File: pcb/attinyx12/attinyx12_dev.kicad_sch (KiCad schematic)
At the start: 28 parts, among them J1 USB_C_Receptacle_USB2.0_16P, J2 Conn_01x06, J3 Conn_01x06, U1 LM321, U2 ATtiny212-SS, U3 CH342K

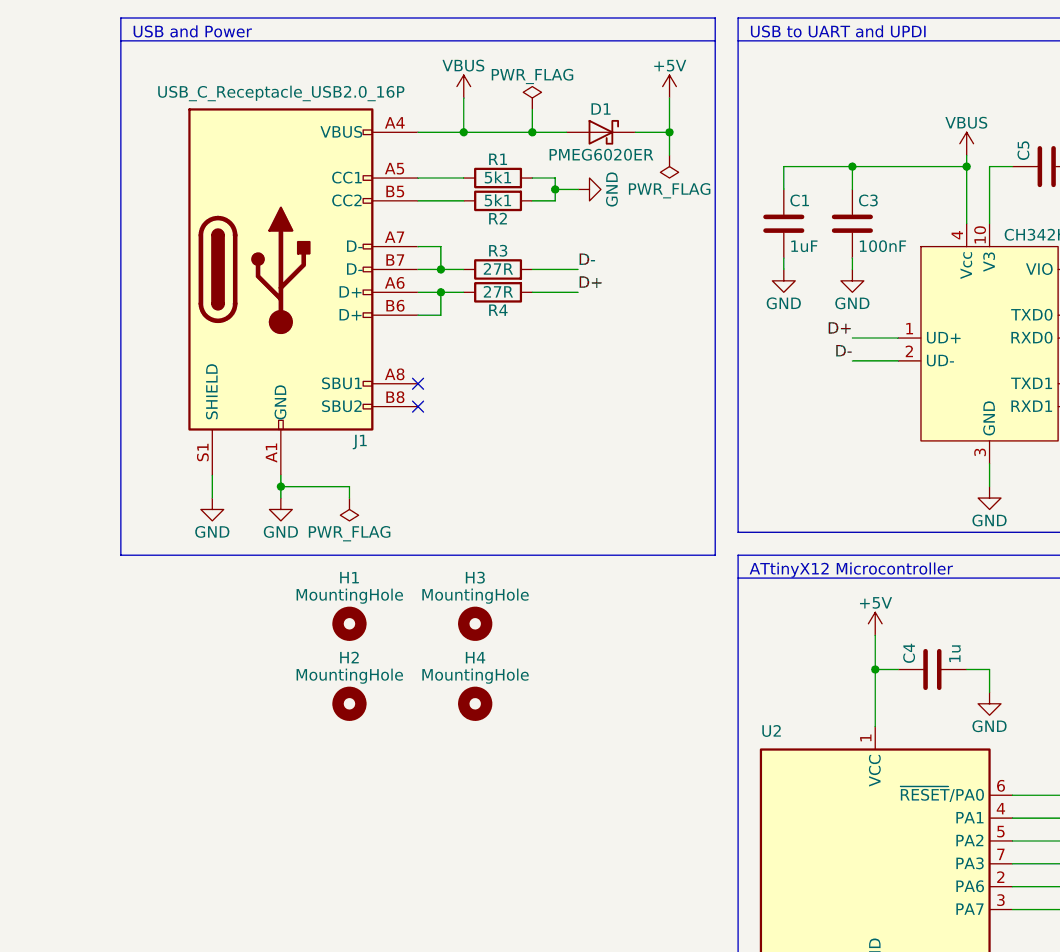
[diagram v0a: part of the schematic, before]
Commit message: polyfuse and TVS+ESD for USB
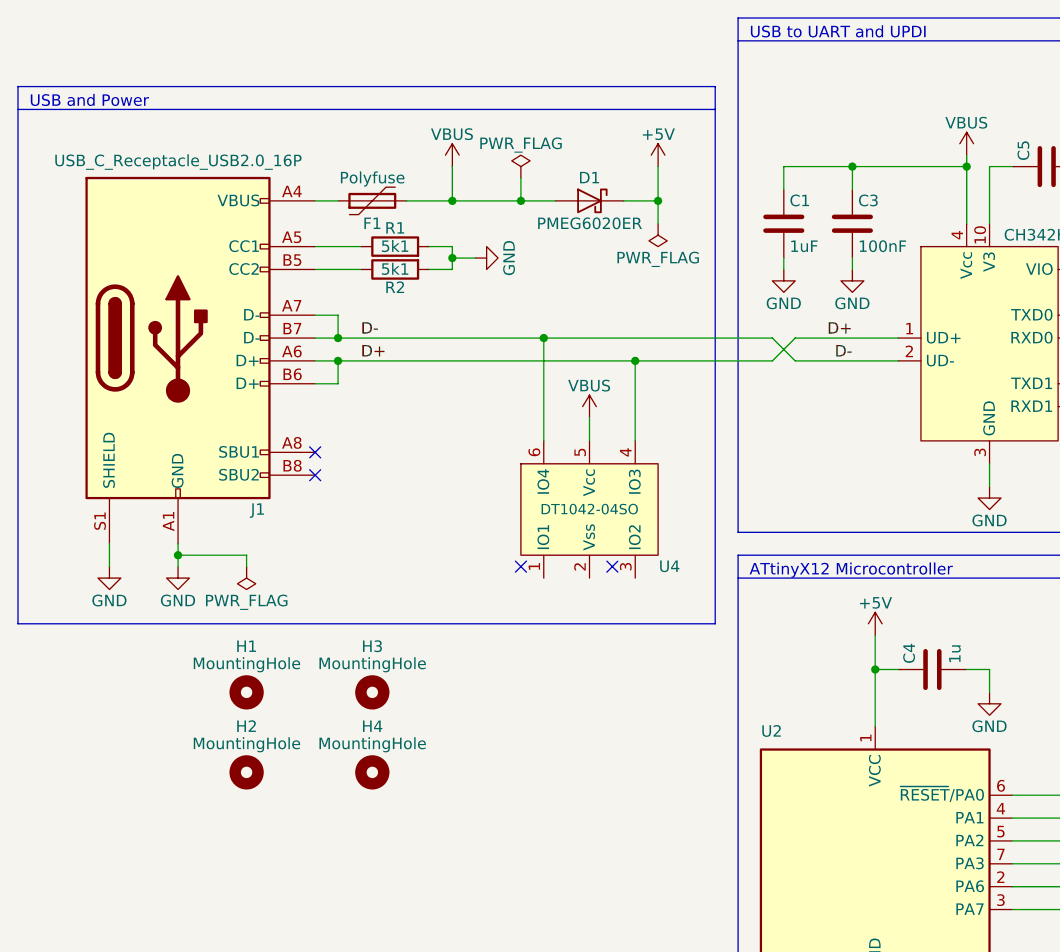
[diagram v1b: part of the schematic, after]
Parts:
- removed R3, R4: 27R, Resistor_SMD:R_0603_1608Metric, symbol Device:R
- added F1: Polyfuse, Fuse:Fuse_0805_2012Metric, symbol Device:Polyfuse
- added U4: DT1042-04SO, Package_TO_SOT_SMD:SOT-23-6, symbol pl_TVS:DT1042-04SO
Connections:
- net D+: now also J1.A6 (D+), J1.B6 (D+), U4.4 (IO3)
- net D-: now also J1.A7 (D-), J1.B7 (D-), U4.6 (IO4)
- net VBUS: now also F1.2, U4.5 (Vcc); no longer J1.A4 (VBUS), J1.A9 (VBUS), J1.B4 (VBUS), J1.B9 (VBUS)
- new net: F1.1, J1.A4 (VBUS), J1.A9 (VBUS), J1.B4 (VBUS), J1.B9 (VBUS)
- no-connect marks 2 -> 4
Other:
- moved on the sheet: D1, H1, H2, H3, H4, J1, R1, R2

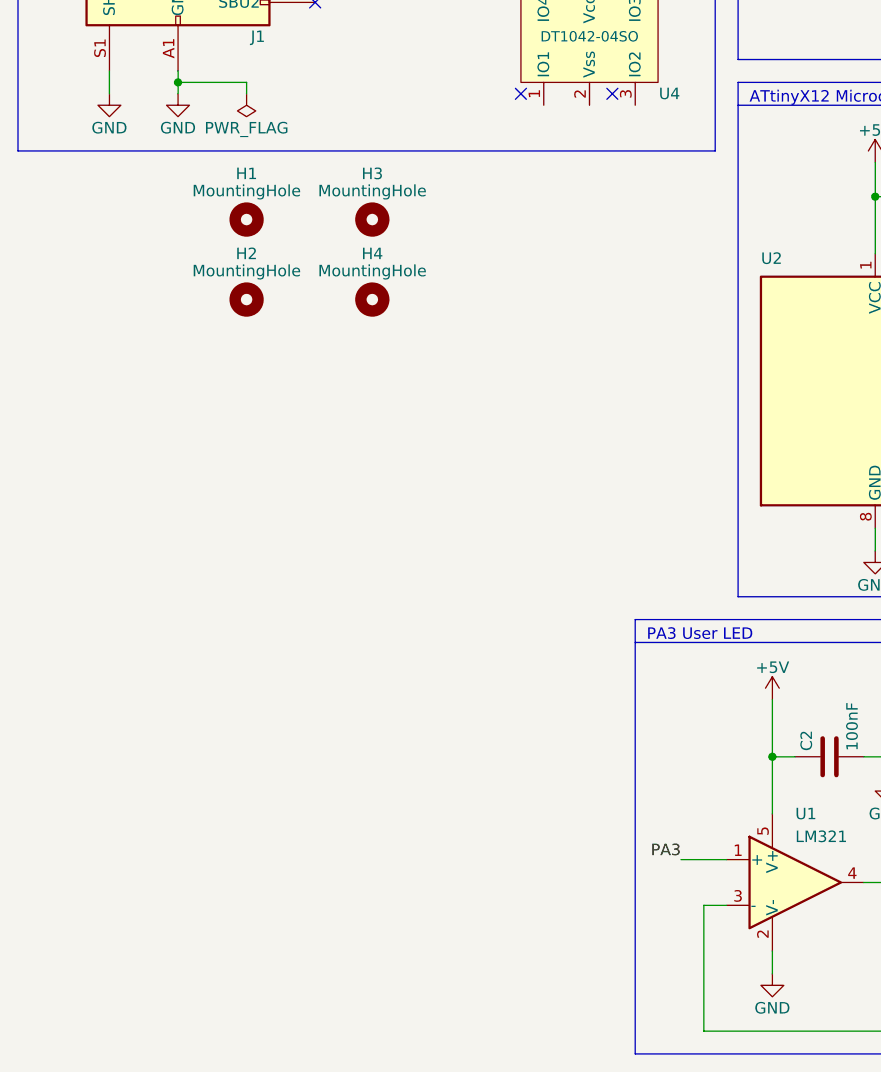
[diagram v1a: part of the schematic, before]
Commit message: add power indicator LED
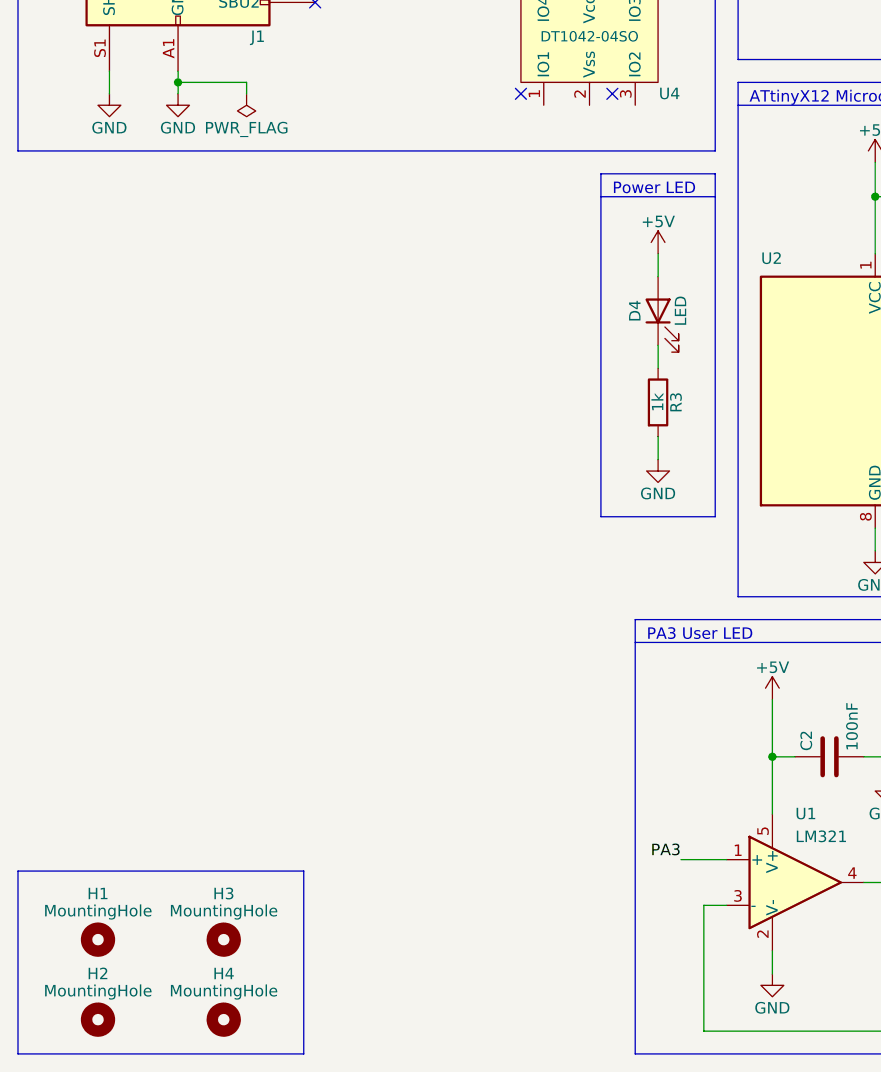
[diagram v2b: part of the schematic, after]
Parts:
- added D4: LED, LED_SMD:LED_0603_1608Metric, symbol Device:LED
- added R3: 1k, Resistor_SMD:R_0603_1608Metric, symbol Device:R
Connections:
- net +5V: now also D4.2 (A)
- net GND: now also R3.2
- new net: D4.1 (K), R3.1
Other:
- note added: "Power LED"
- moved on the sheet: H1, H2, H3, H4

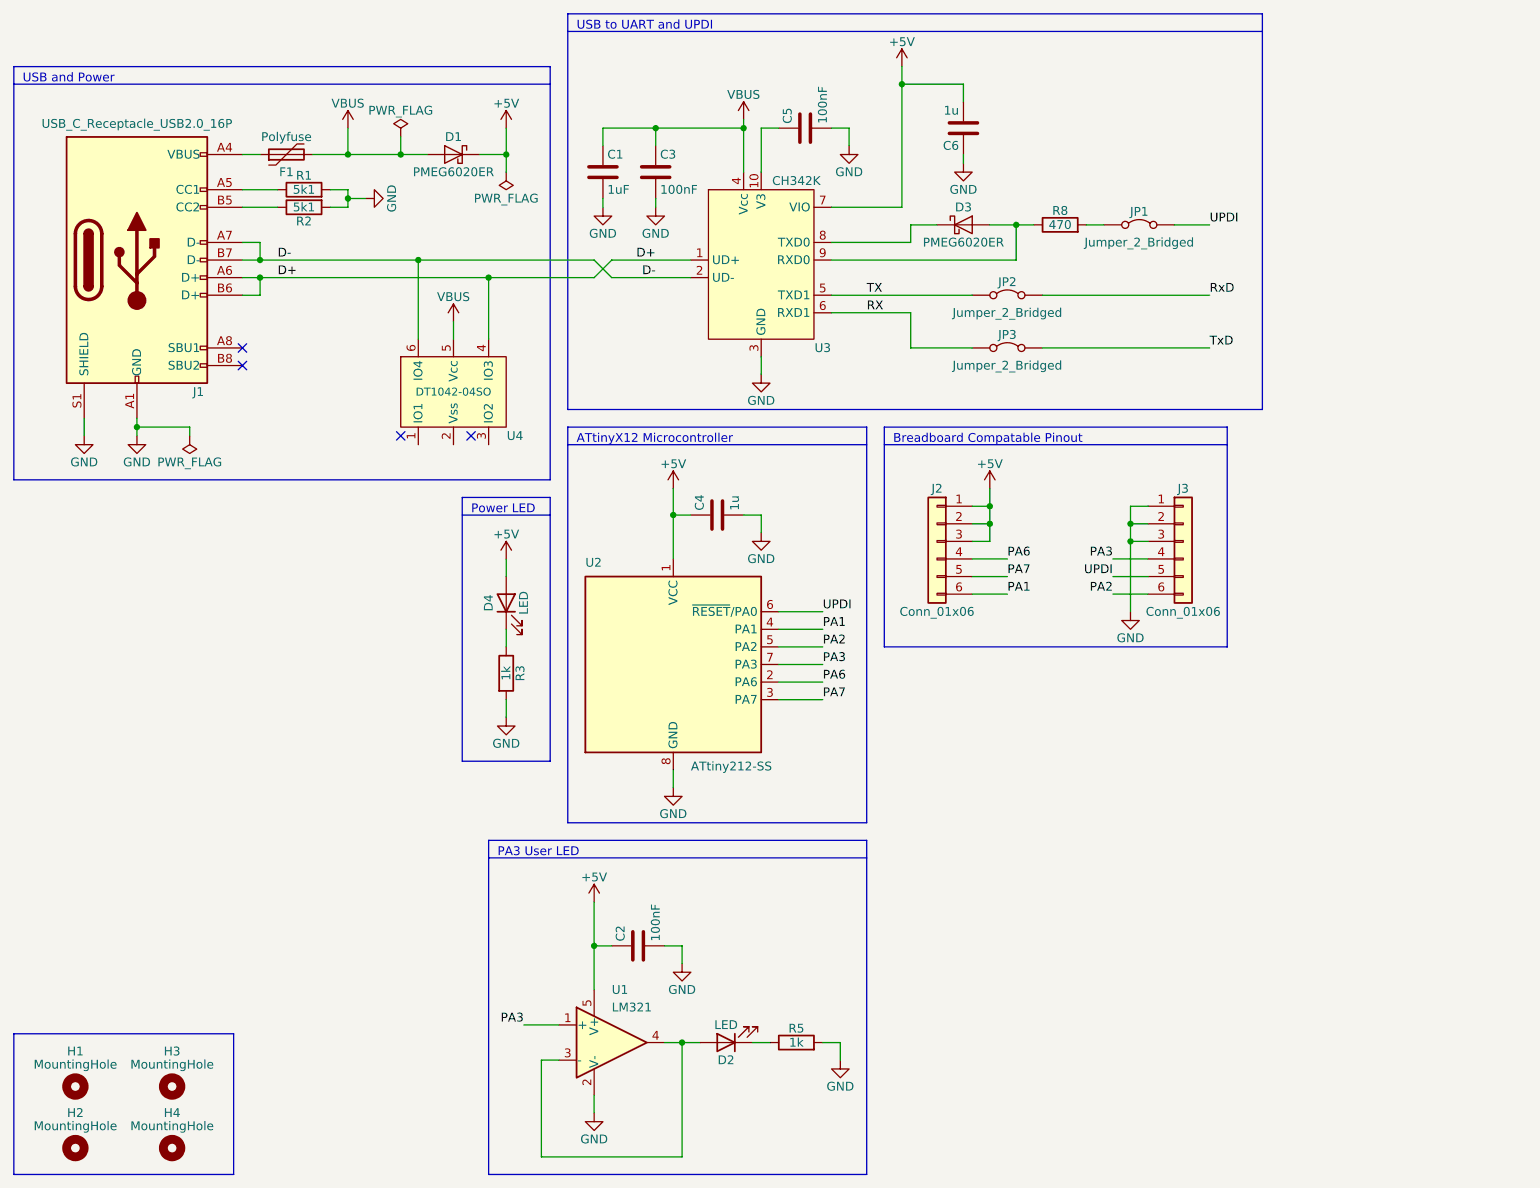
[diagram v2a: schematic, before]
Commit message: TI Launchpad style isolation from programmer
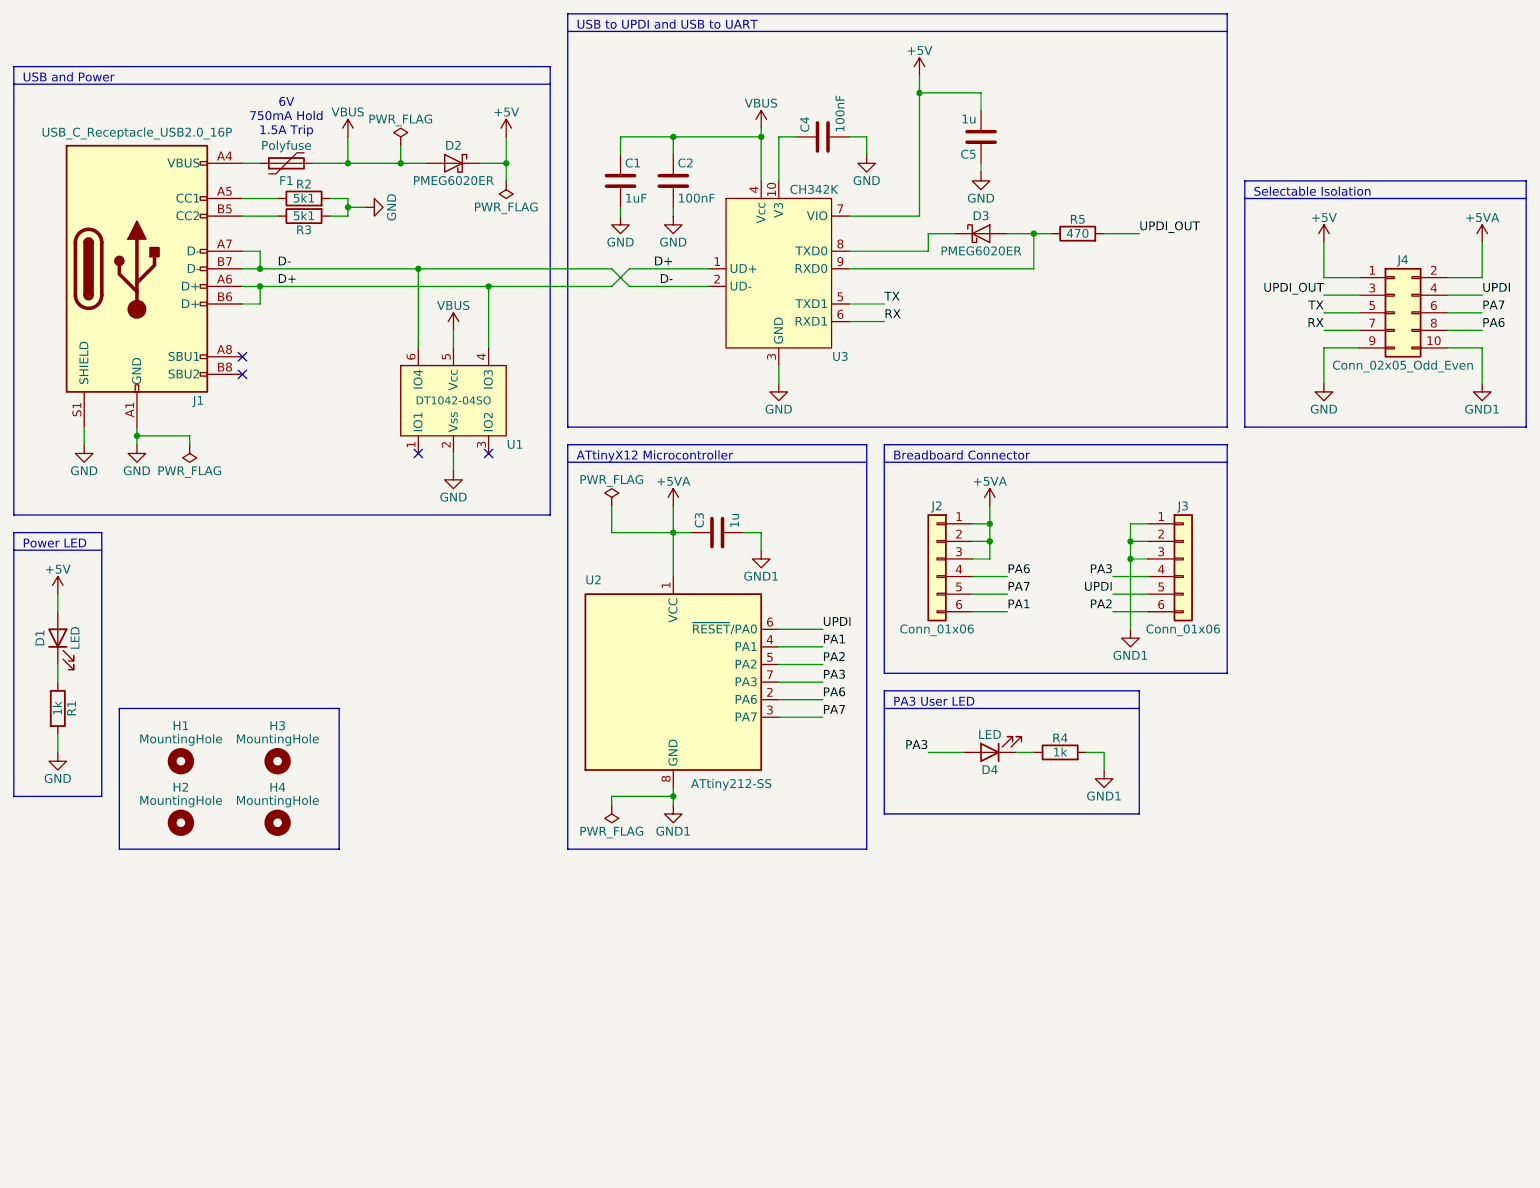
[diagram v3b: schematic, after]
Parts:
- removed C2: 100nF, Capacitor_SMD:C_0603_1608Metric, symbol Device:C
- removed JP1, JP2, JP3: Jumper_2_Bridged, Jumper:SolderJumper-2_P1.3mm_Bridged_RoundedPad1.0x1.5mm, symbol Jumper:Jumper_2_Bridged
- removed U1: LM321, Package_TO_SOT_SMD:SOT-23-5, symbol Amplifier_Operational:LM321
- added J4: Conn_02x05_Odd_Even, Connector_PinHeader_2.54mm:PinHeader_2x05_P2.54mm_Vertical, symbol Connector_Generic:Conn_02x05_Odd_Even
- renumbered C3 to C2, C4 to C3, C5 to C4, C6 to C5, D4 to D1, D1 to D2, D2 to D4, R3 to R1, R1 to R2, R2 to R3, R5 to R4, R8 to R5, U4 to U1
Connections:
- net +5V: now also J4.1 (Pin_1); no longer C3.1, J2.1 (Pin_1), J2.2 (Pin_2), J2.3 (Pin_3), U2.1 (VCC)
- net GND: now also U1.2 (Vss), J4.9 (Pin_9); no longer C3.2, J3.1 (Pin_1), J3.2 (Pin_2), J3.3 (Pin_3), R4.2, U2.8 (GND)
- net PA3: now also D4.2 (A)
- net PA6: now also J4.8 (Pin_8)
- net PA7: now also J4.6 (Pin_6)
- net RX: now also J4.7 (Pin_7)
- net TX: now also J4.5 (Pin_5)
- net UPDI: now also J4.4 (Pin_4)
- net UPDI_OUT: now reaches R5.2
- net UPDI_OUT: now also J4.3 (Pin_3)
- new net +5VA: C3.1, J2.1 (Pin_1), J2.2 (Pin_2), J2.3 (Pin_3), J4.2 (Pin_2), U2.1 (VCC)
- new net GND1: C3.2, J3.1 (Pin_1), J3.2 (Pin_2), J3.3 (Pin_3), J4.10 (Pin_10), R4.2, U2.8 (GND)
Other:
- note added: "6V 750mA Hold 1.5A Trip"
- note added: "Breadboard Connector"
- note added: "Selectable Isolation"
- note added: "USB to UPDI and USB to UART"
- note removed: "Breadboard Compatable Pinout"
- note removed: "USB to UART and UPDI"
- moved on the sheet: C1, C2, C3, C4, C5, D1, D2, D3, D4, F1, H1, H2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
